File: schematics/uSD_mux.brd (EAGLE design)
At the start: 53 x 61 mm, 30 parts

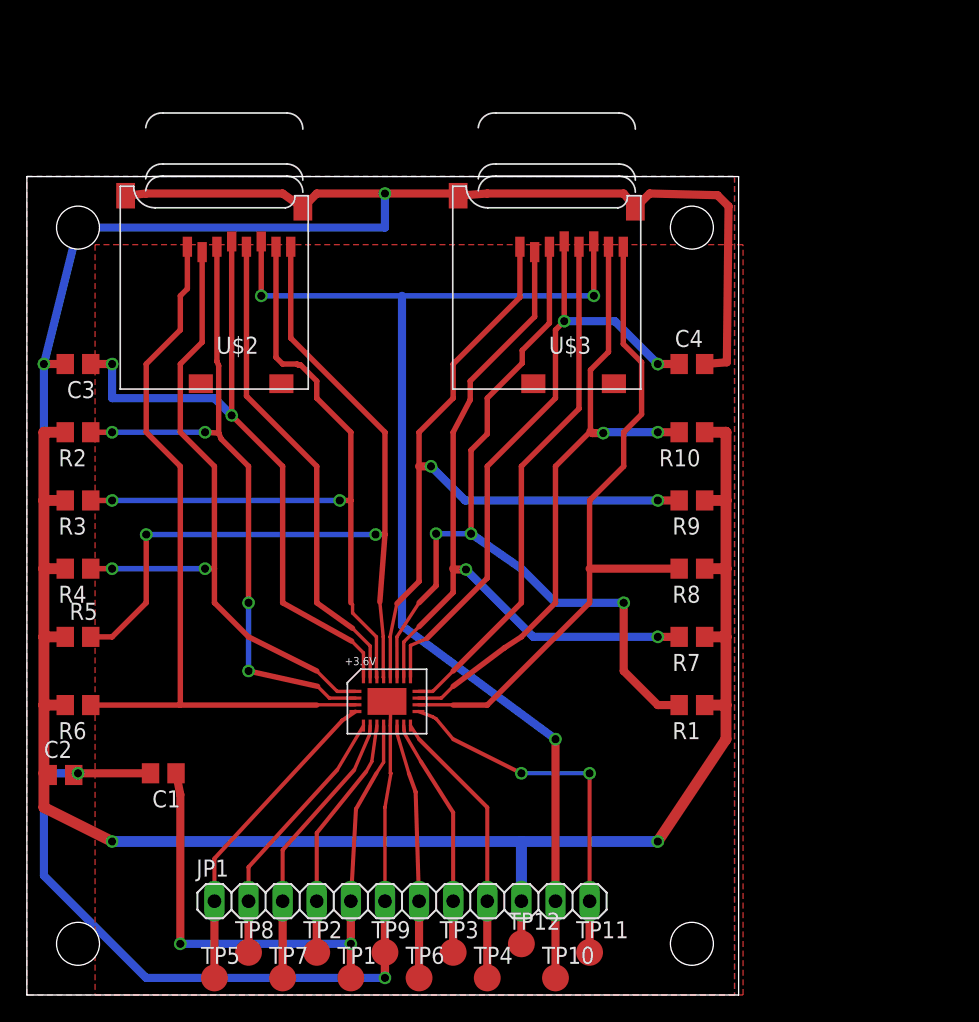
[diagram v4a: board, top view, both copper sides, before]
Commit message: Breakout boards for MUX and uSD socket, updated mux+uSD schematic
Built individual breakout boards for MUX chip and uSD socket.
Discovered errors in MUX and uSD integrated board and updated
schematic--ripped up wrong connections in .brd file but did not bother
rerouting traces since this board will most likely not be fabbed again.
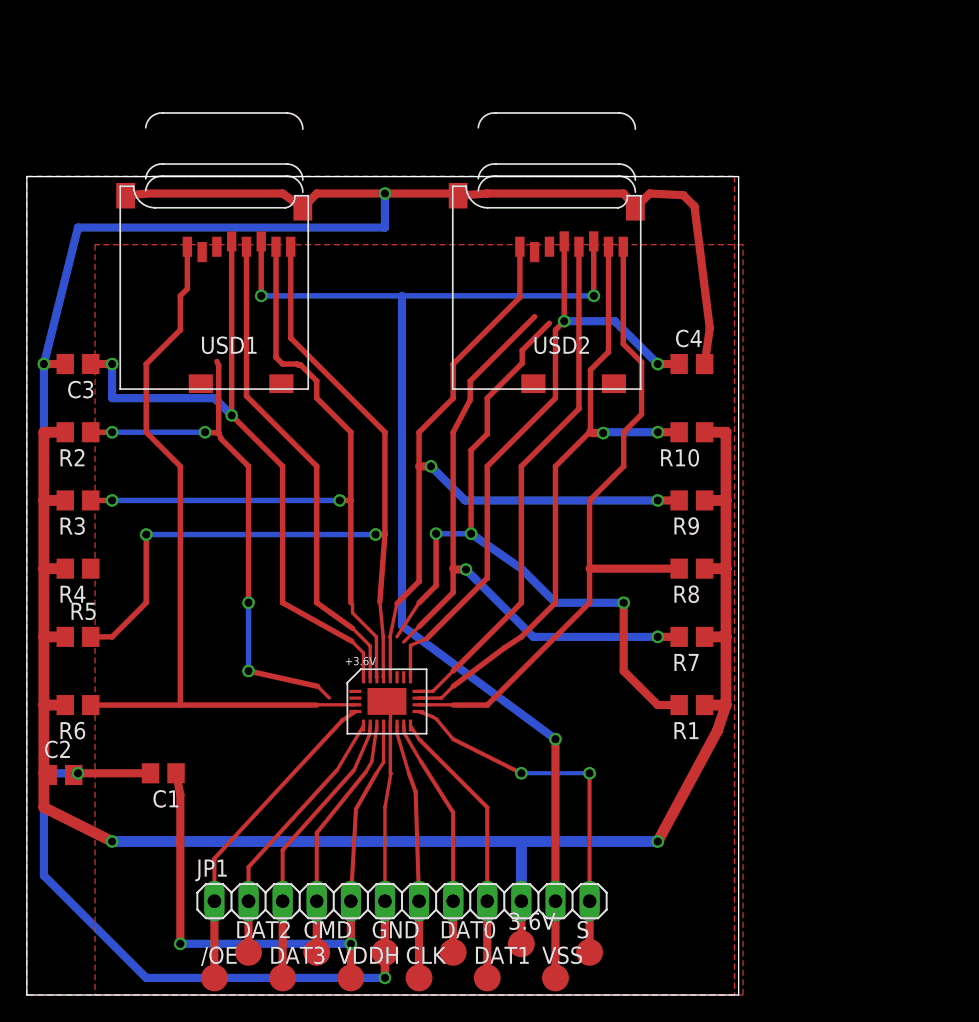
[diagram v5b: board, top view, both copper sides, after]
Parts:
- renumbered TP1 to VDDH, TP10 to VSS, TP11 to S, TP12 to 3.6V, TP2 to CMD, TP3 to DAT0, TP4 to DAT1, TP5 to /OE, TP6 to CLK, TP7 to DAT3, TP8 to DAT2, TP9 to GND, U$2 to USD1, U$3 to USD2
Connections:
- net N$1 renamed +3.6
- removed net N$2: +3.6V.1CMD, R4.1, USD1.2
- new net N$1: +3.6V.1DAT[3], R4.1, USD1.2
- net N$12: now also +3.6V.2CMD; no longer +3.6V.2DAT[3]
- net N$6: now also +3.6V.1CMD; no longer +3.6V.1DAT[3]
- net N$8: now also +3.6V.2DAT[3]; no longer +3.6V.2CMD
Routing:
- net N$2: track 49.8 -> 0.00 mm, vias 2 -> 0
- net N$6: track 50.5 -> 40.0 mm
- net N$12: track 61.6 -> 52.9 mm
- net N$8: track 54.4 -> 47.0 mm
- net GND: track 195.3 -> 191.4 mm
